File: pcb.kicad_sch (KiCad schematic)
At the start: 22 parts, among them J1 USB_B_Micro, J2 3vJumper1, J3 3vJumper1, SW1 RotaryEncoder_Switch_MP, U1 LM1117T-3.3

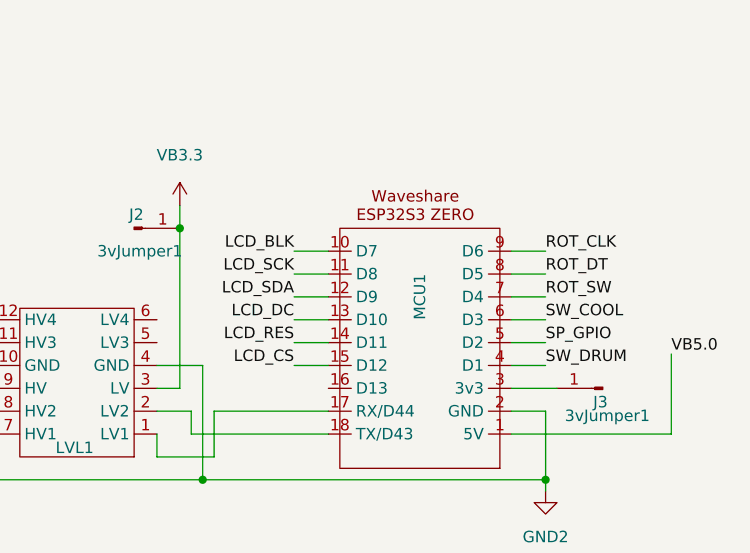
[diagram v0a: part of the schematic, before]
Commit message: updated to support both c3 mini and a c3/S3 zero
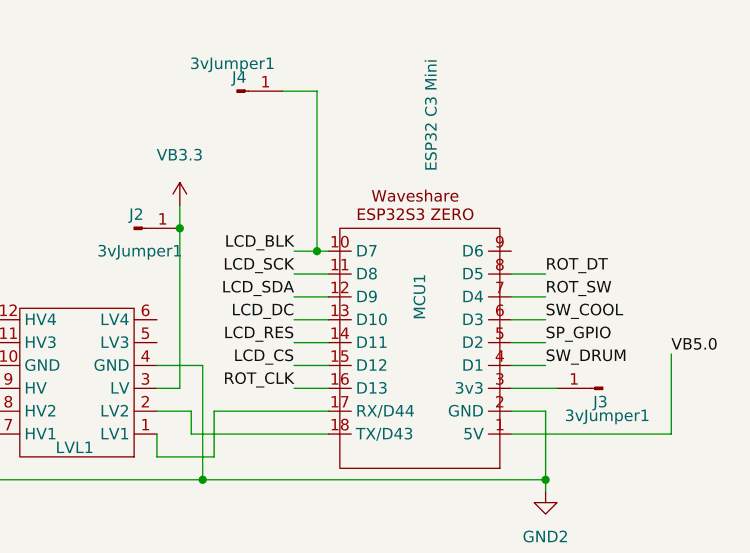
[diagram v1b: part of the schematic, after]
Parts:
- added J4: 3vJumper1, Connector_PinHeader_2.54mm:PinHeader_1x01_P2.54mm_Vertical, symbol Connector:Conn_01x01_Pin
- MCU1: value ~ -> ESP32 C3 Mini
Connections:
- net LCD_BLK: now also J4.1 (Pin_1)
- net ROT_CLK: now also MCU1.16 (D13); no longer MCU1.9 (D6)

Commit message: minor updates
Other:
- company: (none) -> www.kroster.com
- title: (none) -> krostr esp32s3 controller
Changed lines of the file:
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@@
 	(generator_version "8.0")
 	(paper "A4")
+	(title_block
+		(title "krostr esp32s3 controller")
+		(company "www.kroster.com")
+	)
 	(junction
 		(at 163.83 135.89)
